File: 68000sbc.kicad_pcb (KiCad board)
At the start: 2 copper layers, 127 x 90.8 mm, 49 parts, among them J1 USB_B, J2 5V FTDI SERIAL, J3 RTC (SparkFun BOB-10160), J4 CFCARD/IDE, J5 EXPANSION (F.Cu), J6 EXPANSION (B.Cu), SW1 RESET, SW2 BTN1, U1 74HC139, U2 74HC14, U3 TMP68HC000P-12, U4 AS6C4008-55PCN, U5 28C256, U6 AS6C4008-55PCN, U7 28C256, U8 TL16C550, X1 12MHz, X2 12MHz

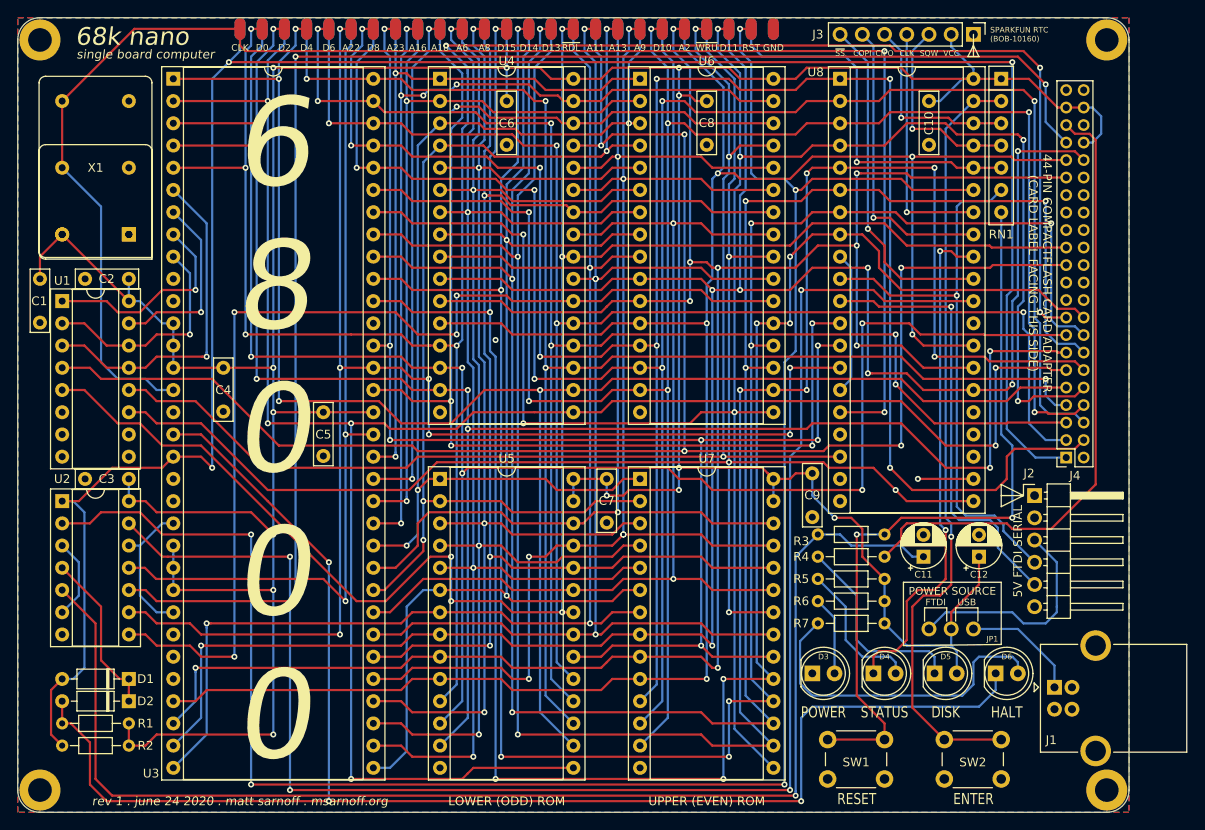
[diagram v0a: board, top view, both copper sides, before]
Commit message: U3,C11,C12をNew_Libraryへ移動
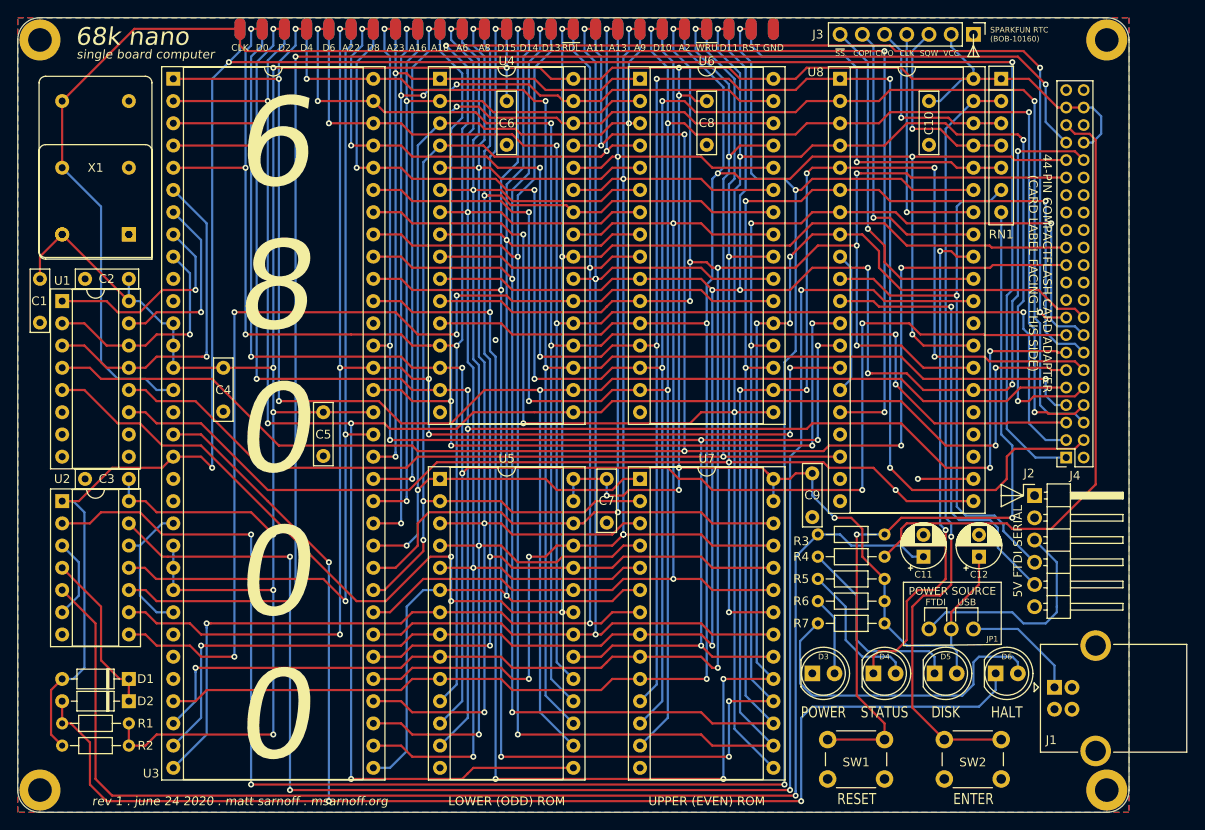
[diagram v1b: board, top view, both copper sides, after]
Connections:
- net /R,~W renamed /R,~{W}
- net /~A20 renamed /~{A20}
- net /~A22 renamed /~{A22}
- net /~AS renamed /~{AS}
- net /~BTN1 renamed /~{BTN1}
- net /~CFLED renamed /~{CFLED}
- net /~HALT renamed /~{HALT}
- net /~IRQ renamed /~{IRQ}
- net /~LDS renamed /~{LDS}
- net /~RDL renamed /~{RDL}
- net /~RDU renamed /~{RDU}
- net /~RESET renamed /~{RESET}
- net /~RESETBTN renamed /~{RESETBTN}
- net /~RTC_SS renamed /~{RTC_SS}
- net /~UDS renamed /~{UDS}
- net /~WRL renamed /~{WRL}
- net /~WRU renamed /~{WRU}
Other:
- net class Default removed
- net class Thicc removed
- board text added: "R/~{W}"
- board text added: "~{AS}"
- board text added: "~{BERR}"
- board text added: "~{BGACK}"
- board text added: "~{BG}"
- board text added: "~{BR}"
- board text added: "~{DTACK}"
- board text added: "~{DTACK} GROUNDED!!"
- board text added: "~{HALT}"
- board text added: "~{IPL0}"
- board text added: "~{IPL1}"
- board text added: "~{IPL2}"
- board text added: "~{LDS}"
- board text added: "~{RDL}"
- board text added: "~{RDU}"
- board text added: "~{RESET}"
- board text added: "~{RST}"
- board text added: "~{SS}"
- board text added: "~{UDS}"
- board text added: "~{VMA}"
- board text added: "~{VPA}"
- board text added: "~{WRL}"
- board text added: "~{WRU}"
- board text removed: "R/~W"
- board text removed: "~AS"
- board text removed: "~BERR"
- board text removed: "~BG"
- board text removed: "~BGACK"
- board text removed: "~BR"
- board text removed: "~DTACK"
- board text removed: "~DTACK~ GROUNDED!!"
- board text removed: "~HALT"
- board text removed: "~IPL0"
- board text removed: "~IPL1"
- board text removed: "~IPL2"
- board text removed: "~LDS"
- board text removed: "~RDL"
- board text removed: "~RDU"
- board text removed: "~RESET"
- board text removed: "~RST"
- board text removed: "~SS"
- board text removed: "~UDS"
- board text removed: "~VMA"
- board text removed: "~VPA"
- board text removed: "~WRL"
- board text removed: "~WRU"
